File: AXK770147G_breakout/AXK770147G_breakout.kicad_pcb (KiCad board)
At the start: 2 copper layers, 63.5 x 48.3 mm, 4 parts, among them J1 Conn_01x35, J2 Conn_01x18, J3 AXK770147G, J4 Conn_01x17

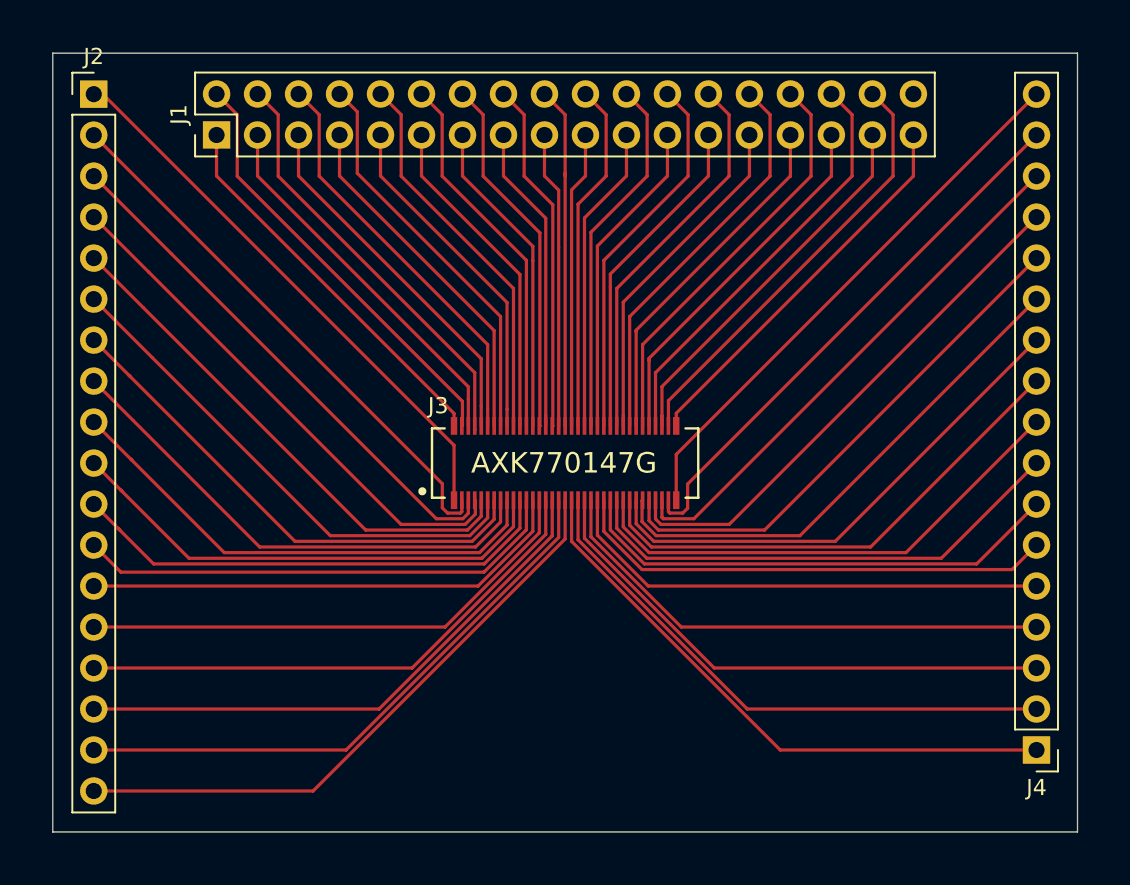
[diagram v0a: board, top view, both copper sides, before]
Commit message: Move traces around a bit to increase separation; add ground pins.
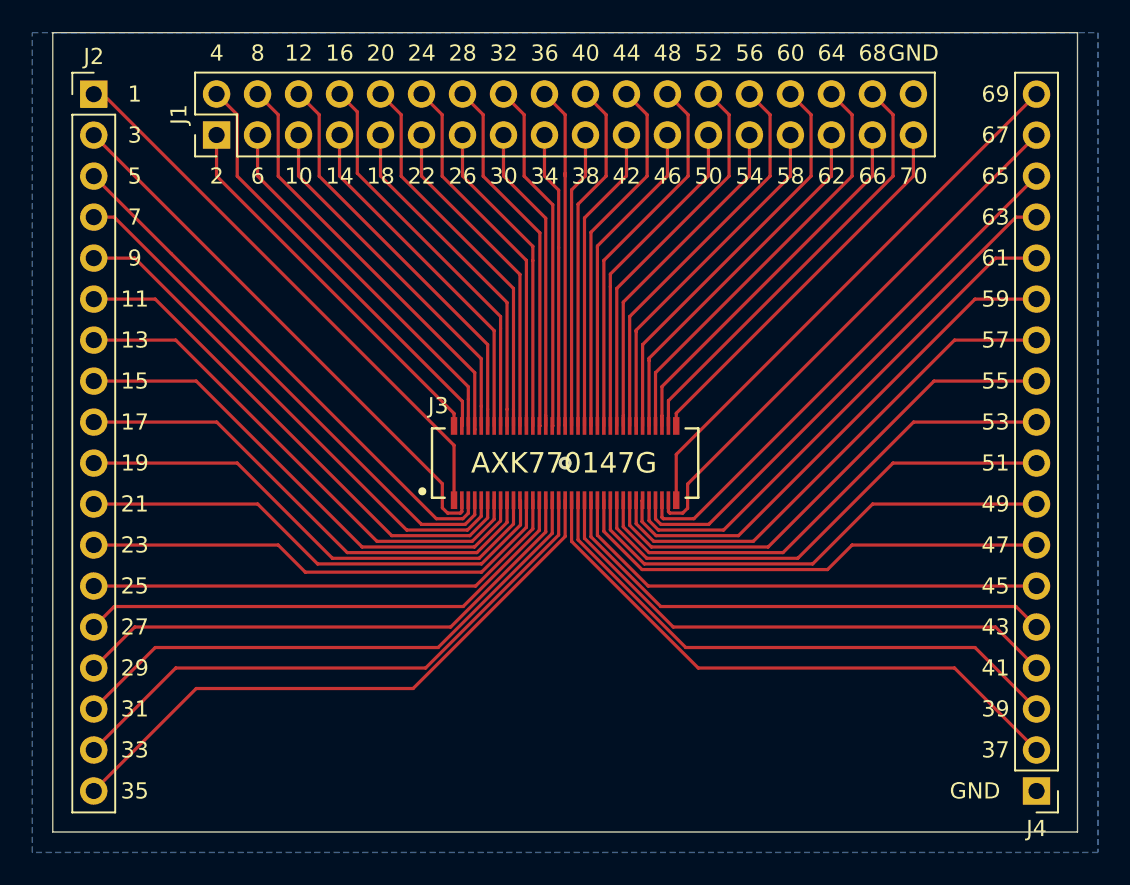
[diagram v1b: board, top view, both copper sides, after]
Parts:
- J1: value Conn_01x35 -> Conn_01x36
- J4: value Conn_01x17 -> Conn_01x18; footprint Connector_PinHeader_2.54mm:PinHeader_1x17_P2.54mm_Vertical -> Connector_PinHeader_2.54mm:PinHeader_1x18_P2.54mm_Vertical
- moved J4 2.54 mm to (350.5, -370.8)
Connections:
- J1 pad 36: (no net) -> GND
- J4 pad 1: Net-(J3-Pad37) -> GND
- J4 pad 10: Net-(J3-Pad55) -> Net-(J3-Pad53)
- J4 pad 11: Net-(J3-Pad57) -> Net-(J3-Pad55)
- J4 pad 12: Net-(J3-Pad59) -> Net-(J3-Pad57)
- J4 pad 13: Net-(J3-Pad61) -> Net-(J3-Pad59)
- J4 pad 14: Net-(J3-Pad63) -> Net-(J3-Pad61)
- J4 pad 15: Net-(J3-Pad65) -> Net-(J3-Pad63)
- J4 pad 16: Net-(J3-Pad67) -> Net-(J3-Pad65)
- J4 pad 17: Net-(J3-Pad69) -> Net-(J3-Pad67)
- J4 pad 2: Net-(J3-Pad39) -> Net-(J3-Pad37)
- J4 pad 3: Net-(J3-Pad41) -> Net-(J3-Pad39)
- J4 pad 4: Net-(J3-Pad43) -> Net-(J3-Pad41)
- J4 pad 5: Net-(J3-Pad45) -> Net-(J3-Pad43)
- J4 pad 6: Net-(J3-Pad47) -> Net-(J3-Pad45)
- J4 pad 7: Net-(J3-Pad49) -> Net-(J3-Pad47)
- J4 pad 8: Net-(J3-Pad51) -> Net-(J3-Pad49)
- J4 pad 9: Net-(J3-Pad53) -> Net-(J3-Pad51)
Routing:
- net GND: vias 0 -> 1
- added copper zone on B.Cu, net GND
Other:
- board size 63.5 x 48.3 mm -> 63.5 x 49.5 mm
- board text added: "1"
- board text added: "10"
- board text added: "11"
- board text added: "12"
- board text added: "13"
- board text added: "14"
- board text added: "15"
- board text added: "16"
- board text added: "17"
- board text added: "18"
- board text added: "19"
- board text added: "2"
- board text added: "20"
- board text added: "21"
- board text added: "22"
- board text added: "23"
- board text added: "24"
- board text added: "25"
- board text added: "26"
- board text added: "27"
- board text added: "28"
- board text added: "29"
- board text added: "3"
- board text added: "30"
- board text added: "31"
- board text added: "32"
- board text added: "33"
- board text added: "34"
- board text added: "35"
- board text added: "36"
- board text added: "37"
- board text added: "38"
- board text added: "39"
- board text added: "4"
- board text added: "40"
- board text added: "41"
- board text added: "42"
- board text added: "43"
- board text added: "44"
- board text added: "45"
- board text added: "46"
- board text added: "47"
- board text added: "48"
- board text added: "49"
- board text added: "5"
- board text added: "50"
- board text added: "51"
- board text added: "52"
- board text added: "53"
- board text added: "54"
- board text added: "55"
- board text added: "56"
- board text added: "57"
- board text added: "58"
- board text added: "59"
- board text added: "6"
- board text added: "60"
- board text added: "61"
- board text added: "62"
- board text added: "63"
- board text added: "64"
- board text added: "65"
- board text added: "66"
- board text added: "67"
- board text added: "68"
- board text added: "69"
- board text added: "7"
- board text added: "70"
- board text added: "8"
- board text added: "9"
- board text added: "GND"
